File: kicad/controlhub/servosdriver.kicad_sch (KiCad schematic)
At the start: 1 part, among them IC1 PCA9685PW

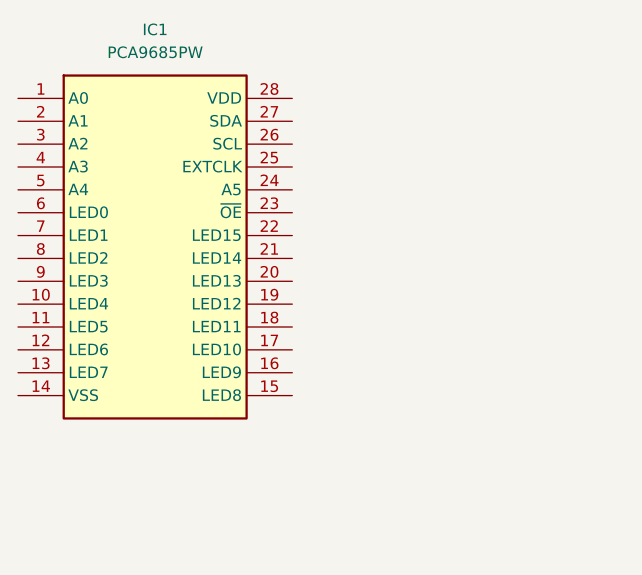
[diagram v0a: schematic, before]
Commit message: fixed drivers issue
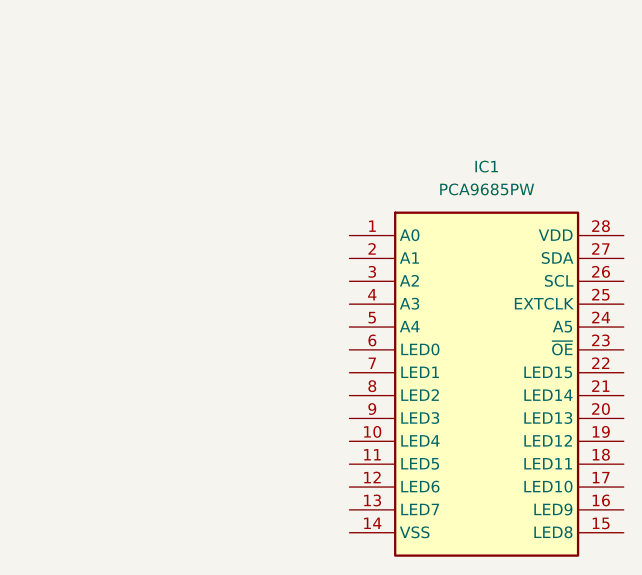
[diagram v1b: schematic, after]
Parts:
- IC1: footprint SOP65P640X110-28N -> Drivers:SOP65P640X110-28N
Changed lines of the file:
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@@
 	(symbol
 		(lib_id "Drivers:PCA9685PW")
-		(at 127 49.53 0)
+		(at 163.83 64.77 0)
 		(unit 1)
 		(exclude_from_sim no)
@@
 		(fields_autoplaced yes)
 		(property "Reference" "IC1"
-			(at 142.24 41.91 0)
+			(at 179.07 57.15 0)
 			(effects
 				(font
@@
 		)
 		(property "Value" "PCA9685PW"
-			(at 142.24 44.45 0)
+			(at 179.07 59.69 0)
 			(effects
 				(font
@@
 			)
 		)
-		(property "Footprint" "SOP65P640X110-28N"
-			(at 153.67 144.45 0)
+		(property "Footprint" "Drivers:SOP65P640X110-28N"
+			(at 190.5 159.69 0)
 			(effects
 				(font
@@
 		)
 		(property "Datasheet" "https://4donline.ihs.com/images/VipMasterIC/IC/PHGL/PHGL-S-A0000775254/PHGL-S-A0000775254-1.pdf?hkey=EF798316E3902B6ED9A73243A3159BB0"
-			(at 153.67 244.45 0)
+			(at 190.5 259.69 0)
 			(effects
 				(font
@@
 		)
 		(property "Description" "LED Display Drivers PCA9685PW/TSSOP28///STANDARD MARKING * IC\\'S TUBE -"
-			(at 127 49.53 0)
+			(at 163.83 64.77 0)
 			(effects
 				(font
@@
 		)
 		(property "Height" "1.1"
-			(at 153.67 444.45 0)
+			(at 190.5 459.69 0)
 			(effects
 				(font
@@
 		)
 		(property "Manufacturer_Name" "NXP"
-			(at 153.67 544.45 0)
+			(at 190.5 559.69 0)
 			(effects
 				(font
@@
 		)
 		(property "Manufacturer_Part_Number" "PCA9685PW"
-			(at 153.67 644.45 0)
+			(at 190.5 659.69 0)
 			(effects
 				(font
@@
 		)
 		(property "Mouser Part Number" "N/A"
-			(at 153.67 744.45 0)
+			(at 190.5 759.69 0)
 			(effects
 				(font
@@
 		)
 		(property "Mouser Price/Stock" "https://www.mouser.co.uk/ProductDetail/NXP-Semiconductors/PCA9685PW/?qs=wXXwzvj5w%252BEzwvjqh1LFVQ%3D%3D"
-			(at 153.67 844.45 0)
+			(at 190.5 859.69 0)
 			(effects
 				(font
@@
 		)
 		(property "Arrow Part Number" ""
-			(at 153.67 944.45 0)
+			(at 190.5 959.69 0)
 			(effects
 				(font
@@
 		)
 		(property "Arrow Price/Stock" ""
-			(at 153.67 1044.45 0)
+			(at 190.5 1059.69 0)
 			(effects
 				(font
@@
 				(hide yes)
 			)
+		)
+		(pin "1"
 		)
 		(pin "2"
@@
 		(pin "15"
 		)
-		(pin "1"
-		)
 		(instances

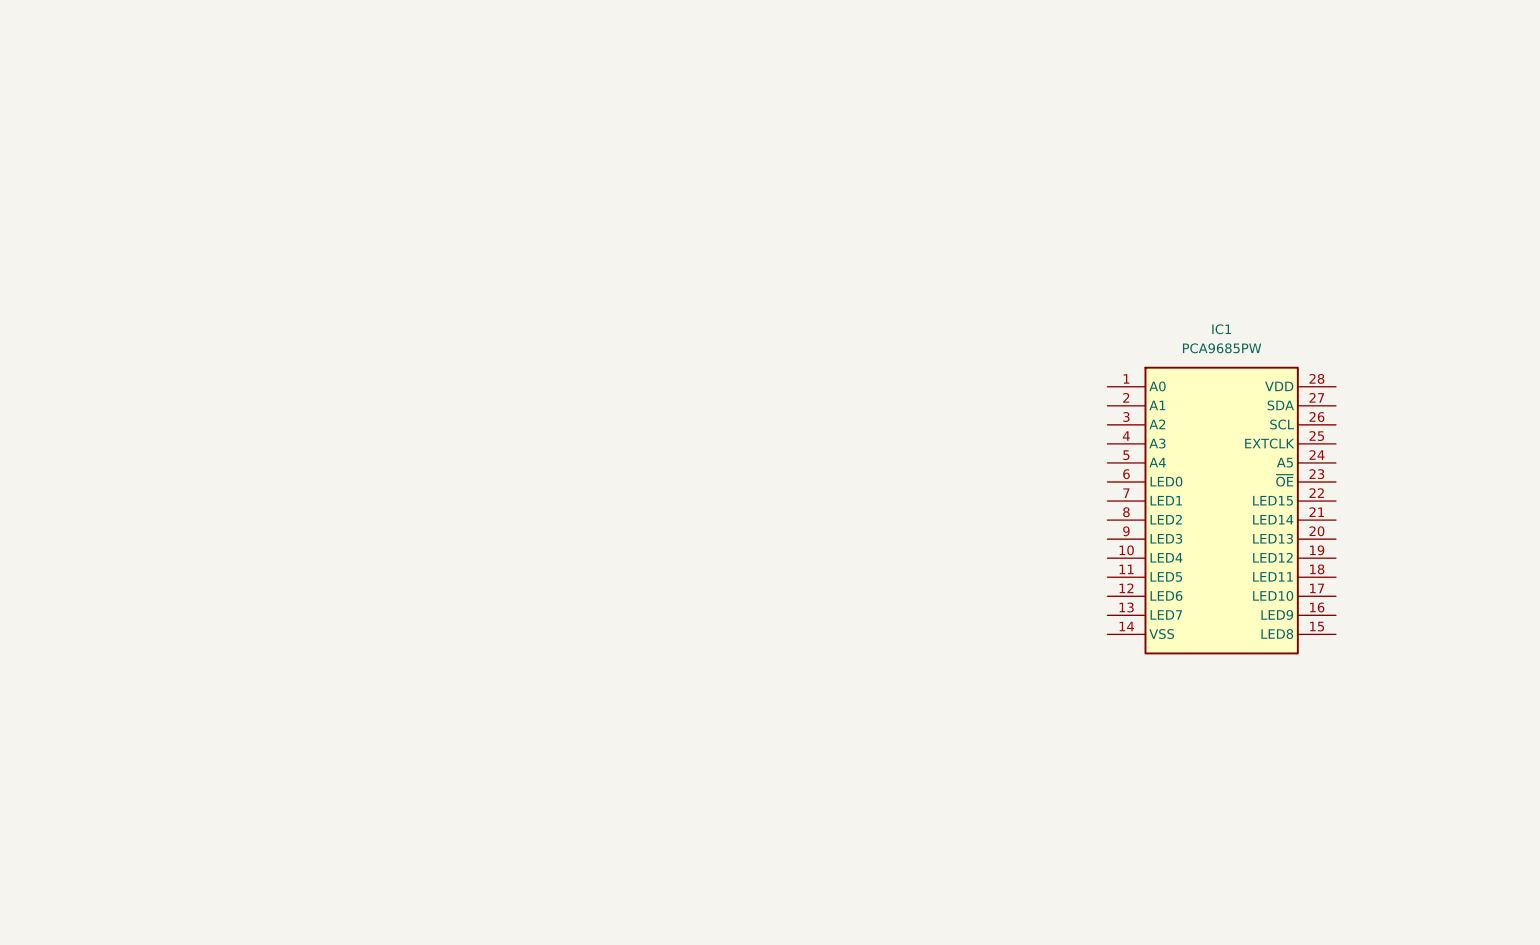
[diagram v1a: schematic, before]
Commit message: fixed library paths
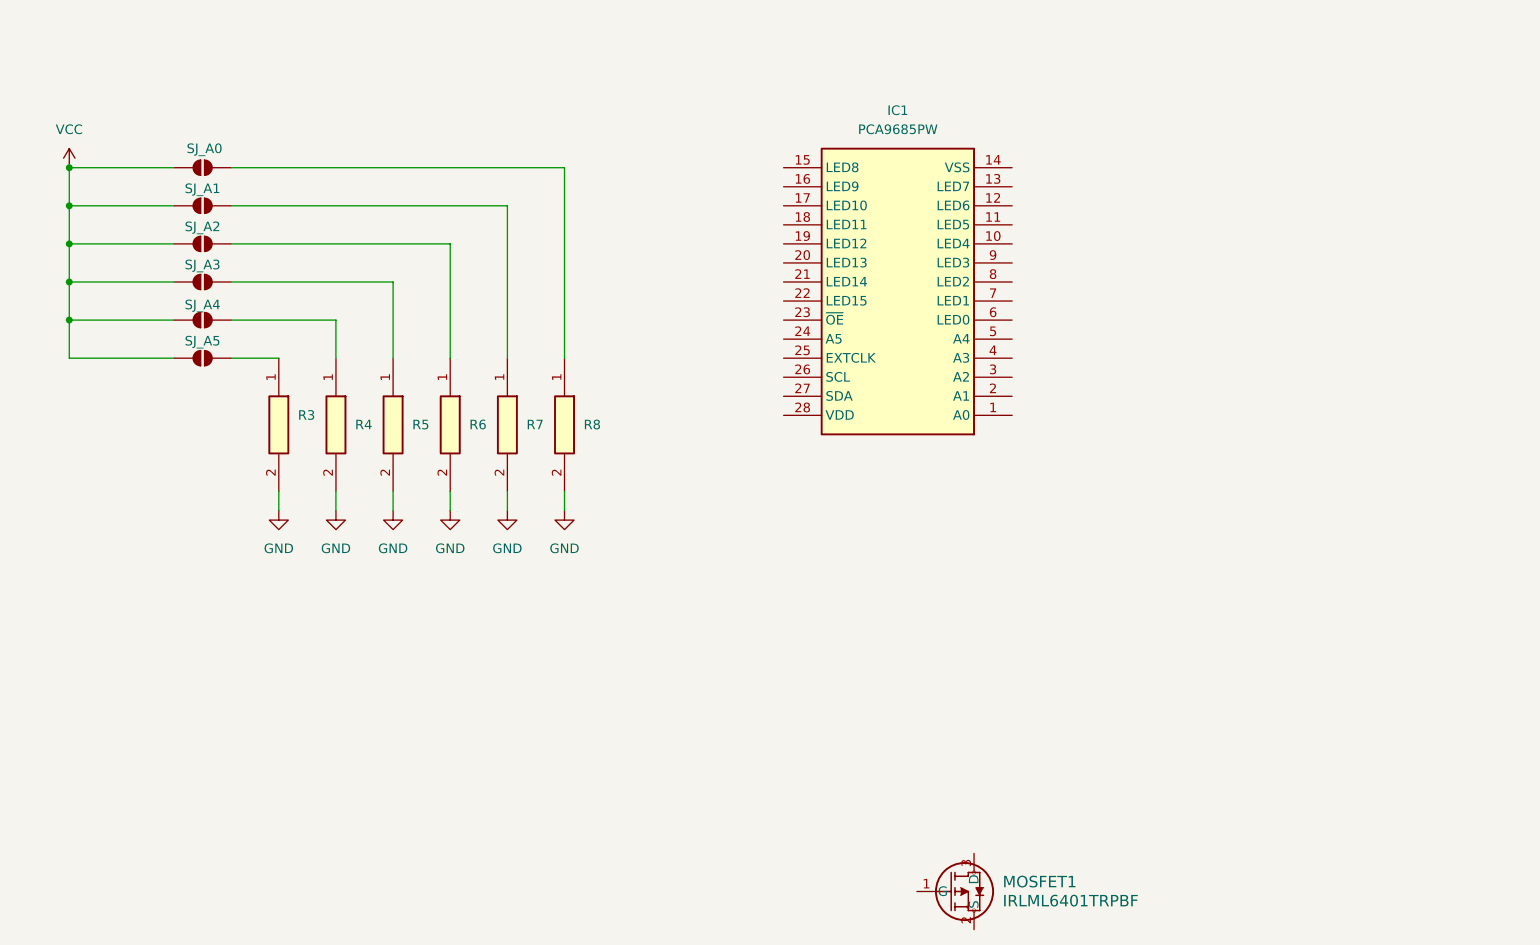
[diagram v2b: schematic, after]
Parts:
- added MOSFET1: IRLML6401TRPBF, Mosfets:MICRO3_SOT23_INF, symbol Mosfets:IRLML6401TRPBF
- added R3, R4, R5, R6, R7, R8: RC0603FR-0710KL, Resistors:RESC1608X55N, symbol Resistors:RC0603FR-0710KL
- added SJ_A0, SJ_A1, SJ_A2, SJ_A3, SJ_A4, SJ_A5: SolderJumper_2_Open, symbol Jumper:SolderJumper_2_Open
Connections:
- new net: R6.1, SJ_A2.2 (B)
- new net: R4.1, SJ_A4.2 (B)
- new net: R3.1, SJ_A5.2 (B)
- new net: R7.1, SJ_A1.2 (B)
- new net: R5.1, SJ_A3.2 (B)
- new net: R8.1, SJ_A0.2 (B)
- new net GND: R3.2, R4.2, R5.2, R6.2, R7.2, R8.2
- new net VCC: SJ_A0.1 (A), SJ_A1.1 (A), SJ_A2.1 (A), SJ_A3.1 (A), SJ_A4.1 (A), SJ_A5.1 (A)
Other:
- moved on the sheet: IC1

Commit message: wrapped up servo driver
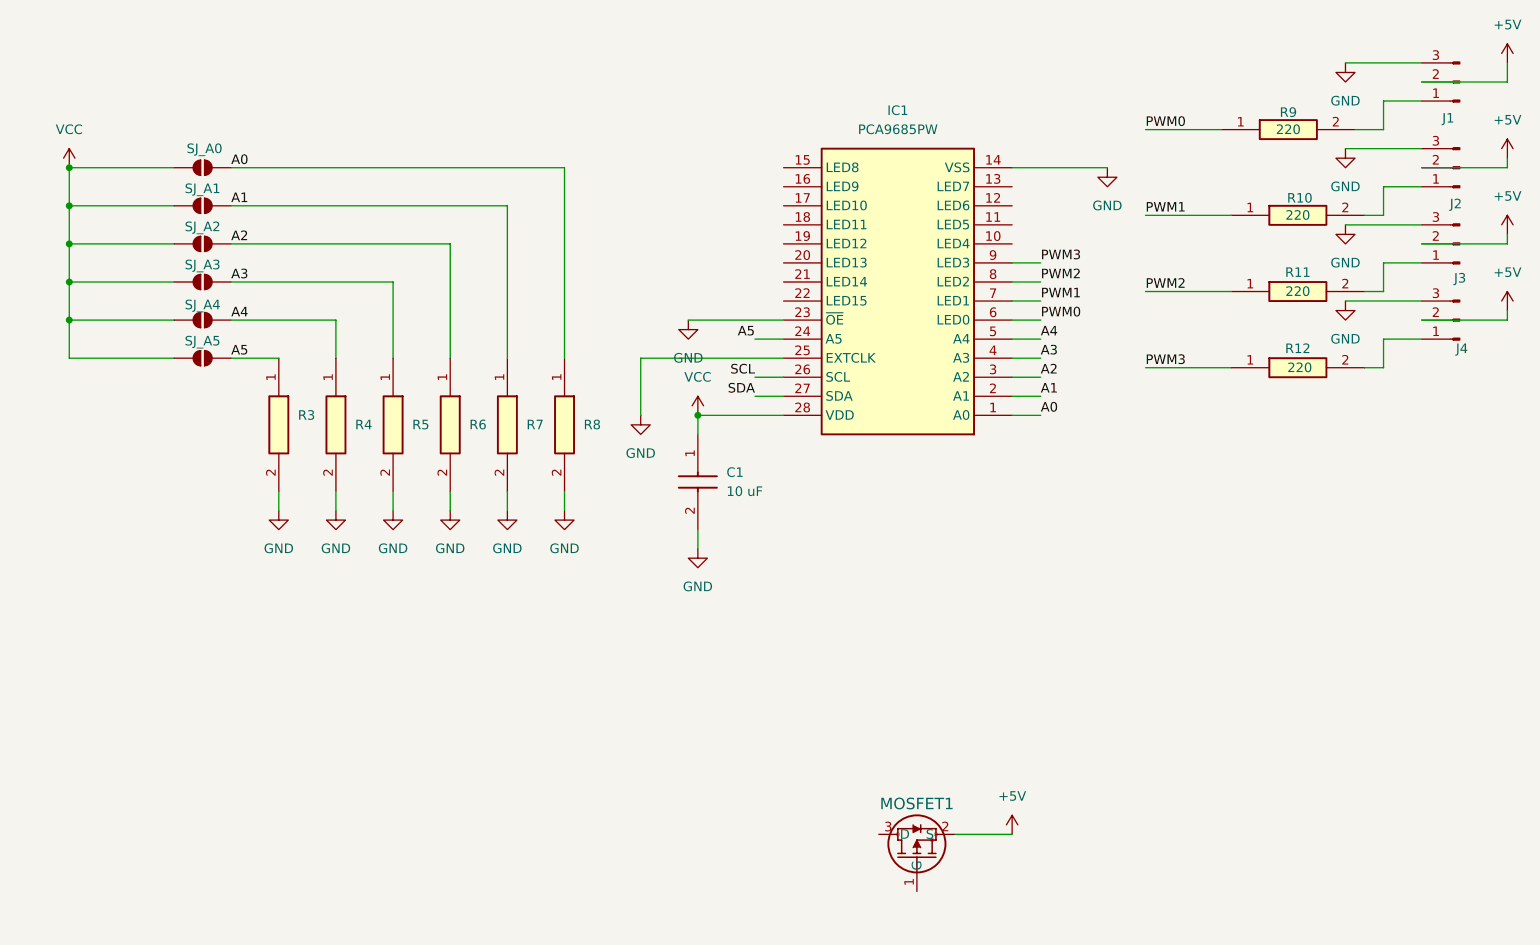
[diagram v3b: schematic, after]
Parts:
- added C1: 10 uF, Capacitors:C0805, symbol Capacitors:C0805C106K8PACTU
- added J1: Conn_01x03_Pin, Connector_PinHeader_2.54mm:PinHeader_1x03_P2.54mm_Horizontal, symbol Connector:Conn_01x03_Pin
- added J2, J3, J4: Conn_01x03_Pin, symbol Connector:Conn_01x03_Pin
- added R10, R11, R12, R9: 220, Resistors:RESC1005X40N, symbol Resistors:RC0402JR-13220RL
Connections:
- net GND: now also IC1.14 (VSS), IC1.23 (~{OE}), IC1.25 (EXTCLK), C1.2, J1.3 (Pin_3), J2.3 (Pin_3), J3.3 (Pin_3), J4.3 (Pin_3)
- net VCC: now also IC1.28 (VDD), C1.1
- net A2: now reaches R6.1, SJ_A2.2 (B)
- net A2: now also IC1.3 (A2)
- net +5V: now reaches MOSFET1.2 (S)
- net +5V: now also J1.2 (Pin_2), J2.2 (Pin_2), J3.2 (Pin_2), J4.2 (Pin_2)
- net A4: now reaches R4.1, SJ_A4.2 (B)
- net A4: now also IC1.5 (A4)
- net A5: now reaches R3.1, SJ_A5.2 (B)
- net A5: now also IC1.24 (A5)
- net A1: now reaches R7.1, SJ_A1.2 (B)
- net A1: now also IC1.2 (A1)
- net A0: now reaches IC1.1 (A0)
- net A0: now also R8.1, SJ_A0.2 (B)
- net SCL: now reaches IC1.26 (SCL)
- net SDA: now reaches IC1.27 (SDA)
- net A3: now reaches IC1.4 (A3)
- net A3: now also R5.1, SJ_A3.2 (B)
- net PWM0: now reaches IC1.6 (LED0)
- net PWM0: now also R9.1
- net PWM1: now reaches IC1.7 (LED1)
- net PWM1: now also R10.1
- net PWM2: now reaches IC1.8 (LED2)
- net PWM2: now also R11.1
- net PWM3: now reaches IC1.9 (LED3)
- net PWM3: now also R12.1
- new net: J3.1 (Pin_1), R11.2
- new net: J4.1 (Pin_1), R12.2
- new net: J2.1 (Pin_1), R10.2
- new net: J1.1 (Pin_1), R9.2
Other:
- moved on the sheet: MOSFET1

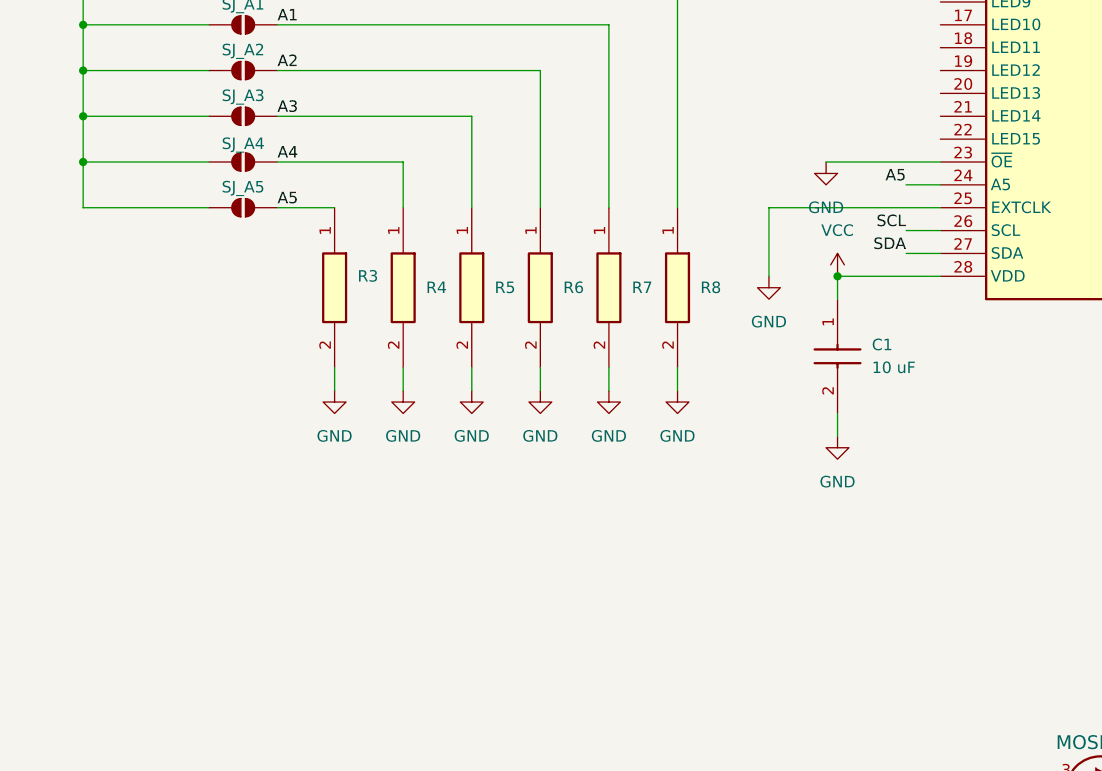
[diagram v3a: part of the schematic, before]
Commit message: removed uneccesary schematics and worked on proper wiring
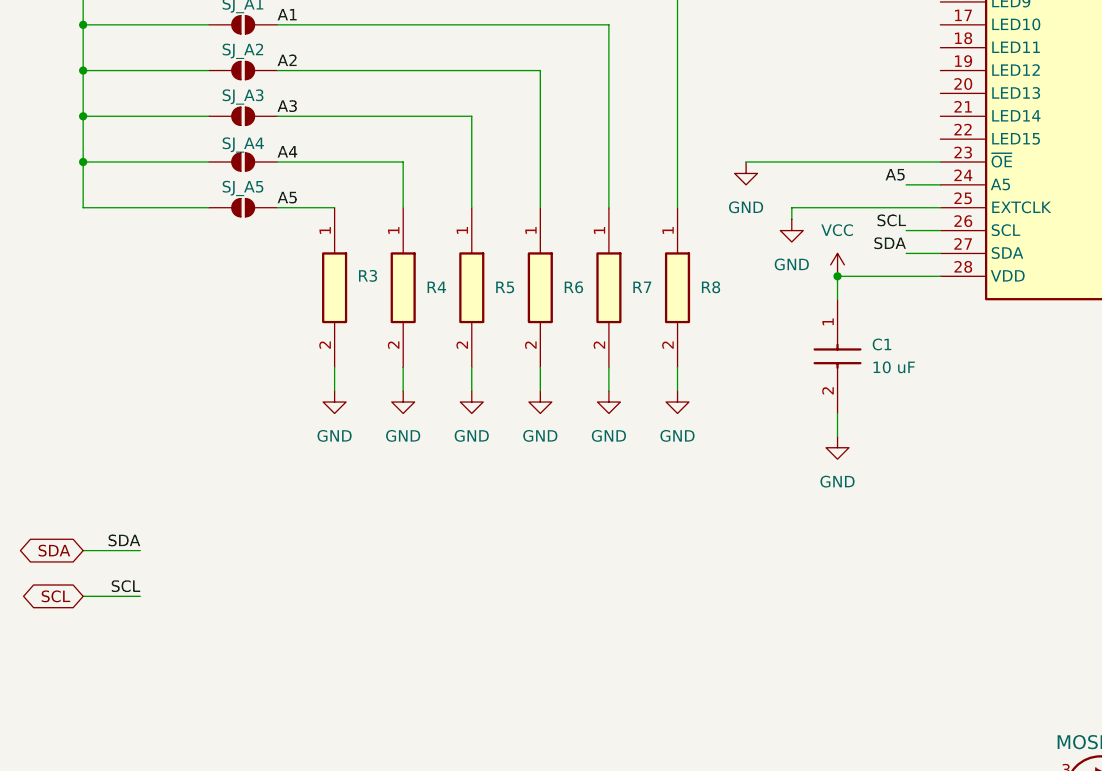
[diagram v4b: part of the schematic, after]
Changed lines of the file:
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@@
 	(wire
 		(pts
+			(xy 25.4 99.06) (xy 31.75 99.06)
+		)
+		(stroke
+			(width 0)
+			(type default)
+		)
+	)
+	(wire
+		(pts
 			(xy 83.82 78.74) (xy 83.82 81.28)
 		)
@@
 	(wire
 		(pts
-			(xy 107.95 55.88) (xy 120.65 55.88)
+			(xy 99.06 55.88) (xy 120.65 55.88)
 		)
 		(stroke
@@
 	(wire
 		(pts
+			(xy 25.4 104.14) (xy 31.75 104.14)
+		)
+		(stroke
+			(width 0)
+			(type default)
+		)
+	)
+	(wire
+		(pts
 			(xy 217.17 35.56) (xy 217.17 34.29)
 		)
@@
 	(wire
 		(pts
-			(xy 101.6 60.96) (xy 101.6 68.58)
+			(xy 104.14 60.96) (xy 104.14 62.23)
 		)
 		(stroke
@@
 	(wire
 		(pts
-			(xy 120.65 60.96) (xy 101.6 60.96)
+			(xy 120.65 60.96) (xy 104.14 60.96)
 		)
 		(stroke
@@
 		)
 	)
+	(label "SCL"
+		(at 31.75 104.14 180)
+		(effects
+			(font
+				(size 1.27 1.27)
+			)
+			(justify right bottom)
+		)
+	)
 	(label "PWM1"
 		(at 168.91 41.91 0)
@@
 		)
 	)
+	(label "SDA"
+		(at 31.75 99.06 180)
+		(effects
+			(font
+				(size 1.27 1.27)
+			)
+			(justify right bottom)
+		)
+	)
+	(global_label "SCL"
+		(shape bidirectional)
+		(at 25.4 104.14 180)
+		(fields_autoplaced yes)
+		(effects
+			(font
+				(size 1.27 1.27)
+			)
+			(justify right)
+		)
+		(property "Intersheetrefs" "${INTERSHEET_REFS}"
+			(at 18.6089 104.14 0)
+			(effects
+				(font
+					(size 1.27 1.27)
+				)
+				(justify right)
+				(hide yes)
+			)
+		)
+	)
+	(global_label "SDA"
+		(shape bidirectional)
+		(at 25.4 99.06 180)
+		(fields_autoplaced yes)
+		(effects
+			(font
+				(size 1.27 1.27)
+			)
+			(justify right)
+		)
+		(property "Intersheetrefs" "${INTERSHEET_REFS}"
+			(at 18.5484 99.06 0)
+			(effects
+				(font
+					(size 1.27 1.27)
+				)
+				(justify right)
+				(hide yes)
+			)
+		)
+	)
 	(symbol
 		(lib_id "Jumper:SolderJumper_2_Open")
@@
 	(symbol
 		(lib_id "power:GND")
-		(at 101.6 68.58 0)
+		(at 104.14 62.23 0)
 		(unit 1)
 		(exclude_from_sim no)
@@
 		(fields_autoplaced yes)
 		(property "Reference" "#PWR022"
-			(at 101.6 74.93 0)
+			(at 104.14 68.58 0)
 			(effects
 				(font
@@
 		)
 		(property "Value" "GND"
-			(at 101.6 73.66 0)
+			(at 104.14 67.31 0)
 			(effects
 				(font
@@
 		)
 		(property "Footprint" ""
-			(at 101.6 68.58 0)
+			(at 104.14 62.23 0)
 			(effects
 				(font
@@
 		)
 		(property "Datasheet" ""
-			(at 101.6 68.58 0)
+			(at 104.14 62.23 0)
 			(effects
 				(font
@@
 		)
 		(property "Description" "Power symbol creates a global label with name \"GND\" , ground"
-			(at 101.6 68.58 0)
+			(at 104.14 62.23 0)
 			(effects
 				(font
@@
 	(symbol
 		(lib_id "power:GND")
-		(at 107.95 55.88 0)
+		(at 99.06 55.88 0)
 		(unit 1)
 		(exclude_from_sim no)
@@
 		(fields_autoplaced yes)
 		(property "Reference" "#PWR024"
-			(at 107.95 62.23 0)
+			(at 99.06 62.23 0)
 			(effects
 				(font
@@
 		)
 		(property "Value" "GND"
-			(at 107.95 60.96 0)
+			(at 99.06 60.96 0)
 			(effects
 				(font
@@
 		)
 		(property "Footprint" ""
-			(at 107.95 55.88 0)
+			(at 99.06 55.88 0)
 			(effects
 				(font
@@
 		)
 		(property "Datasheet" ""
-			(at 107.95 55.88 0)
+			(at 99.06 55.88 0)
 			(effects
 				(font
@@
 		)
 		(property "Description" "Power symbol creates a global label with name \"GND\" , ground"
-			(at 107.95 55.88 0)
+			(at 99.06 55.88 0)
 			(effects
 				(font
